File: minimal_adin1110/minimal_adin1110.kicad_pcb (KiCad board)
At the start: 4 copper layers, 45.1 x 27.9 mm, 70 parts, among them J1 CLP-112-02-G-D-BE, J2 CLP-102-02-G-D-BE, J3 CLP-102-02-G-D-BE, J4 CLP-102-02-G-D-BE, J5 CLP-102-02-G-D-BE, U1 ADIN1110CCPZ, Y1 FA-128 25.0000MF20X-K0

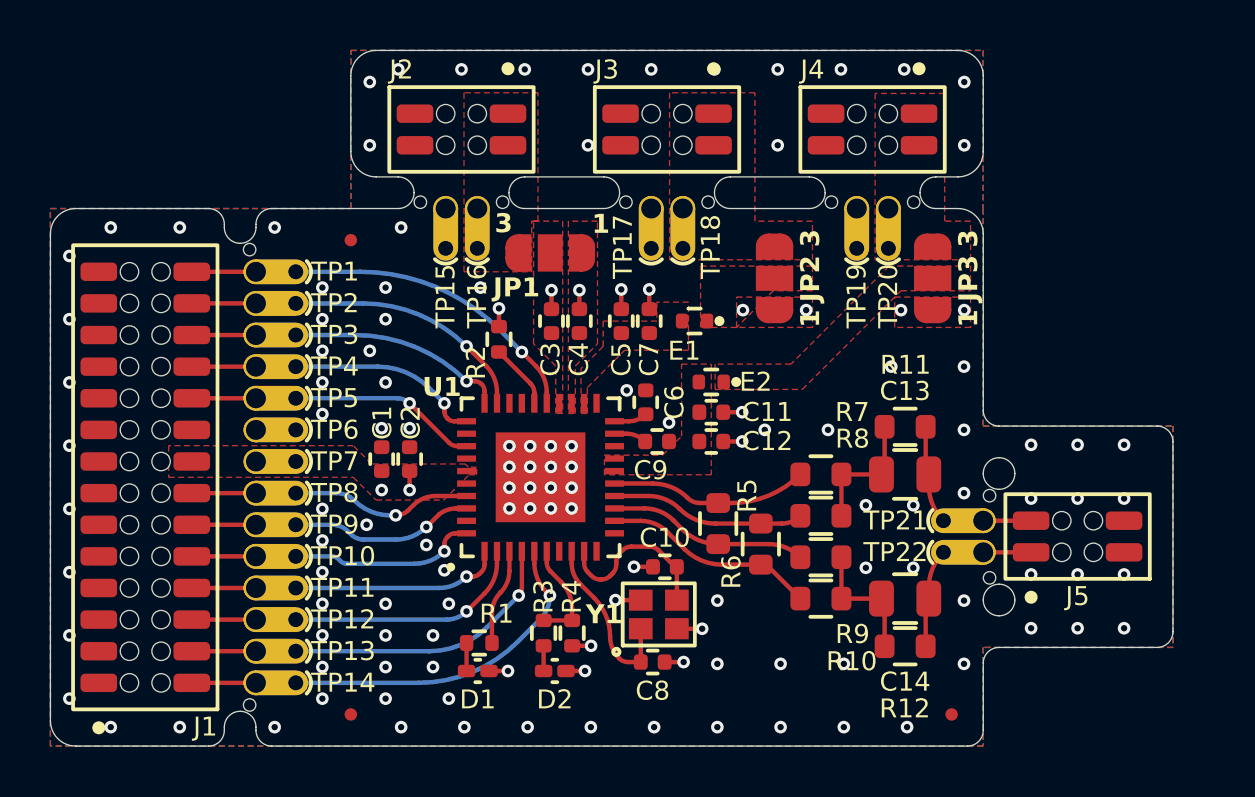
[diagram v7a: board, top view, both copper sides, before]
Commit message: Update KiCAD subproject commit and adjust pad dimensions
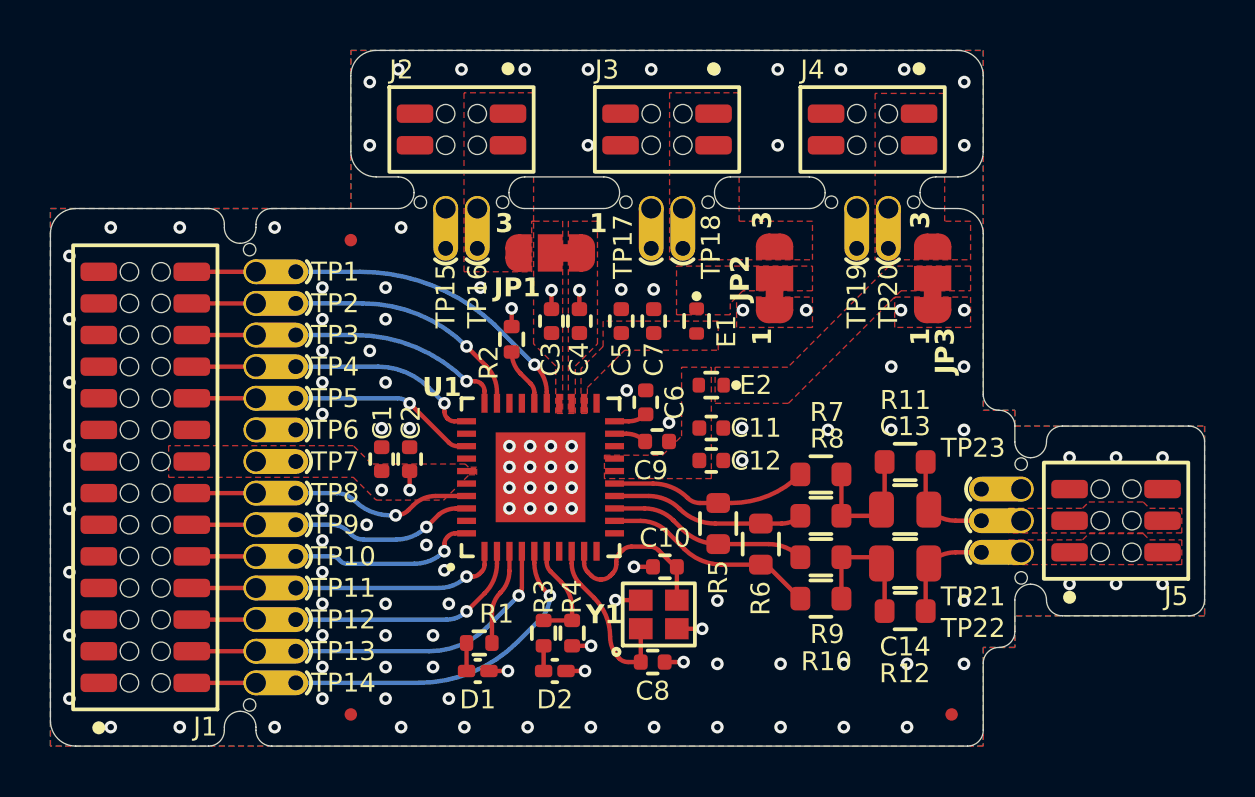
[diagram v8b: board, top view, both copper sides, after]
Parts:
- added TP23: TestPoint, test_point_footprints:TestPoint_THTPad_Castelated, F.Cu at (151.1, 87.6)
- C1, C11, C4, C6, C7: value 0.1uF -> 100 nF
- C12, C2, C5: value 0.01 uF -> 10 nF
- C13, C14: value 2.2 uF -> 220 nF
- C9: value 1 uF -> 1 µF
- D1, D2: value APHHS1005CGCK -> 1.8 V
- J1: value CLP-112-02-G-D-BE -> CLP-114-02-G-D-BE
- J5: value CLP-102-02-G-D-BE -> CLP-103-02-G-D-BE; footprint connector_footprints:CLP-102-02-G-D-BE -> connector_footprints:CLP-103-02-G-D-BE
- JP1, JP2, JP3: footprint solder_jumper_footprints:SolderJumper-3_P1.3mm_Open_RoundedPad1.0x1.5mm_NumberLabels -> solder_jumper_footprints:SolderJumper-3_P1.3mm_Bridged_1_2_RoundedPad1.0x1.5mm_NumberLabels
- MB5: footprint mouse_bite_footprints:mouse-bite-midle-50mil-200mil -> mouse_bite_footprints:mouse-bite-midle-50mil-250mil
- R1, R3: value 4.7k -> 4.7 kΩ
- R10, R7: value 49.9 -> 49.9 Ω
- R11, R12: value 1Meg -> 1 MΩ
- R2: value 1.5k -> 1.5 kΩ
- R4, R5, R6: value 10k -> 10 kΩ
- R8, R9: value 4.99k -> 4.99 kΩ
- Y1: value FA-128 25.0000MF20X-K0 -> 25.0000MHz
- moved J5 1.67 mm to (154.9, 88.9)
- moved TP21 1.52 mm to (151.1, 88.9)
- moved TP22 1.52 mm to (151.1, 90.1)
- moved MB5 1.42 mm to (151.5, 88.9), turned to 90 degrees
- moved R11 1.41 mm to (146.5, 86.5)
- moved C13 1.41 mm to (146.5, 88.4)
- moved C14 1.41 mm to (146.5, 90.6)
- moved R12 1.41 mm to (146.5, 92.5)
- moved C12 0.76 mm to (138.7, 86.4)
- moved C11 0.63 mm to (138.7, 85.1)
- moved R2 0.51 mm to (130.7, 81.6)
- moved C7 0.18 mm to (136.4, 80.8)
- moved E2 0.13 mm to (138.7, 83.4)
- moved E1 0.08 mm to (138.1, 80.8), turned to -90 degrees
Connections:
- J5 pad 2: GND -> /DATA_AND_POWER_N
- J5 pad 4: GND -> /DATA_AND_POWER_P
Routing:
- net GND: track 8.19 -> 5.08 mm, vias 125 -> 115
- net /DATA_AND_POWER_N: track 5.89 -> 4.19 mm
- net /DATA_AND_POWER_P: track 5.89 -> 4.19 mm
- added copper zone on F.Cu, net /DATA_AND_POWER_N
- added copper zone on F.Cu, net /DATA_AND_POWER_P
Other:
- board size 45.1 x 27.9 mm -> 46.4 x 27.9 mm
